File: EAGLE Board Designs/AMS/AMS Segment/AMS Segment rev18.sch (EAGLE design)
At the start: 161 parts, among them J1 CONNECTOR-2_MICROFIT_SMD_RIGH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, J10 CONNECTOR-2_MICROFIT_SMD_RIGH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, J100 CONNECTOR-1_5222_, J101 CONNECTOR-1_5222_, J102 CONNECTOR-1_5222_, J103 CONNECTOR-1_5222_, J104 CONNECTOR-1_5222_, J105 CONNECTOR-1_5222_, J106 CONNECTOR-1_5222_, J107 CONNECTOR-1_5222_, J108 CONNECTOR-1_5222_, J109 CONNECTOR-1_5222_, J110 CONNECTOR-1_5222_, J111 CONNECTOR-1_5222_, J112 CONNECTOR-1_5222_, J113 CONNECTOR-1_5222_, J114 CONNECTOR-1_5222_, J115 CONNECTOR-1_5222_, J116 CONNECTOR-1_5222_, J117 CONNECTOR-1_5222_, J118 CONNECTOR-1_5222_, J119 CONNECTOR-1_5222_, J120 CONNECTOR-1_5222_, J121 CONNECTOR-1_5222_, J2 CONNECTOR-2_MICROFIT_SMD_RIGH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, J3 CONNECTOR-2_MICROFIT_SMD_RIGH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, J4 CONNECTOR-2_MICROFIT_SMD_RIGH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, J5 CONNECTOR-2_MICROFIT_SMD_RIGH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, J6 CONNECTOR-2_MICROFIT_SMD_RIGH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, J7 CONNECTOR-2_MICROFIT_SMD_RIGH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, J8 CONNECTOR-2_MICROFIT_SMD_RIGH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, J9 CONNECTOR-2_MICROFIT_SMD_RIGH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, T1 TRANSFORMER_HM2112ZNLT, U1 SHT31-ARP-B, U2 LTC6811-2, U3 LT3990-5, U4 LT3990-5, U5 LTC6811-2, U6 SHT31-ARP-B

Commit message: Prepped rev 18 with updated lib
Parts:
- J100, J101, J102, J103, J104, J105, J106, J107, J108, J109, J110, J111, J112, J113, J114, J115, J116, J117, J118, J119, J120, J121: value CONNECTOR-1_5222_ -> CONNECTOR-1_5222; device HyTechDevices:CONNECTOR-1_5222_ -> HyTechDevices:CONNECTOR-1_5222
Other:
- note removed: "The LT3990-5 implementation precisely follows the LTC6811-2 datasheet recommendation."
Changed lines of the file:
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@@
 <attribute name="REVIEWER_SCHEMATIC" value="Ethan Weinstock"/>
 </part>
-<part name="Q1" library="HyTechDevices" deviceset="TRANSISTOR_P_MOS_?_*" device="SOT23" technology="SI2369DS-T1-GE3"/>
+<part name="Q1" library="HyTechDevices" deviceset="TRANSISTOR_P_MOS_?_*" device="SOT-23" technology="SI2369DS-T1-GE3"/>
 </parts>
 <sheets>
@@
 <part name="F18" library="HyTechDevices" deviceset="FUSE_?_*" device="0885" technology="1" value="FUSE_0885_1"/>
 <part name="F21" library="HyTechDevices" deviceset="FUSE_?_*" device="0885" technology="1" value="FUSE_0885_1"/>
-<part name="J101" library="HyTechDevices" deviceset="CONNECTOR-1_?_*" device="5222"/>
-<part name="J100" library="HyTechDevices" deviceset="CONNECTOR-1_?_*" device="5222"/>
-<part name="J102" library="HyTechDevices" deviceset="CONNECTOR-1_?_*" device="5222"/>
-<part name="J103" library="HyTechDevices" deviceset="CONNECTOR-1_?_*" device="5222"/>
-<part name="J104" library="HyTechDevices" deviceset="CONNECTOR-1_?_*" device="5222"/>
-<part name="J105" library="HyTechDevices" deviceset="CONNECTOR-1_?_*" device="5222"/>
-<part name="J106" library="HyTechDevices" deviceset="CONNECTOR-1_?_*" device="5222"/>
-<part name="J107" library="HyTechDevices" deviceset="CONNECTOR-1_?_*" device="5222"/>
-<part name="J108" library="HyTechDevices" deviceset="CONNECTOR-1_?_*" device="5222"/>
-<part name="J109" library="HyTechDevices" deviceset="CONNECTOR-1_?_*" device="5222"/>
-<part name="J110" library="HyTechDevices" deviceset="CONNECTOR-1_?_*" device="5222"/>
-<part name="J111" library="HyTechDevices" deviceset="CONNECTOR-1_?_*" device="5222"/>
-<part name="J112" library="HyTechDevices" deviceset="CONNECTOR-1_?_*" device="5222"/>
-<part name="J113" library="HyTechDevices" deviceset="CONNECTOR-1_?_*" device="5222"/>
-<part name="J114" library="HyTechDevices" deviceset="CONNECTOR-1_?_*" device="5222"/>
-<part name="J115" library="HyTechDevices" deviceset="CONNECTOR-1_?_*" device="5222"/>
-<part name="J116" library="HyTechDevices" deviceset="CONNECTOR-1_?_*" device="5222"/>
-<part name="J117" library="HyTechDevices" deviceset="CONNECTOR-1_?_*" device="5222"/>
-<part name="J118" library="HyTechDevices" deviceset="CONNECTOR-1_?_*" device="5222"/>
-<part name="J119" library="HyTechDevices" deviceset="CONNECTOR-1_?_*" device="5222"/>
-<part name="J120" library="HyTechDevices" deviceset="CONNECTOR-1_?_*" device="5222"/>
-<part name="J121" library="HyTechDevices" deviceset="CONNECTOR-1_?_*" device="5222"/>
+<part name="J101" library="HyTechDevices" deviceset="CONNECTOR-1_?" device="5222"/>
+<part name="J100" library="HyTechDevices" deviceset="CONNECTOR-1_?" device="5222"/>
+<part name="J102" library="HyTechDevices" deviceset="CONNECTOR-1_?" device="5222"/>
+<part name="J103" library="HyTechDevices" deviceset="CONNECTOR-1_?" device="5222"/>
+<part name="J104" library="HyTechDevices" deviceset="CONNECTOR-1_?" device="5222"/>
+<part name="J105" library="HyTechDevices" deviceset="CONNECTOR-1_?" device="5222"/>
+<part name="J106" library="HyTechDevices" deviceset="CONNECTOR-1_?" device="5222"/>
+<part name="J107" library="HyTechDevices" deviceset="CONNECTOR-1_?" device="5222"/>
+<part name="J108" library="HyTechDevices" deviceset="CONNECTOR-1_?" device="5222"/>
+<part name="J109" library="HyTechDevices" deviceset="CONNECTOR-1_?" device="5222"/>
+<part name="J110" library="HyTechDevices" deviceset="CONNECTOR-1_?" device="5222"/>
+<part name="J111" library="HyTechDevices" deviceset="CONNECTOR-1_?" device="5222"/>
+<part name="J112" library="HyTechDevices" deviceset="CONNECTOR-1_?" device="5222"/>
+<part name="J113" library="HyTechDevices" deviceset="CONNECTOR-1_?" device="5222"/>
+<part name="J114" library="HyTechDevices" deviceset="CONNECTOR-1_?" device="5222"/>
+<part name="J115" library="HyTechDevices" deviceset="CONNECTOR-1_?" device="5222"/>
+<part name="J116" library="HyTechDevices" deviceset="CONNECTOR-1_?" device="5222"/>
+<part name="J117" library="HyTechDevices" deviceset="CONNECTOR-1_?" device="5222"/>
+<part name="J118" library="HyTechDevices" deviceset="CONNECTOR-1_?" device="5222"/>
+<part name="J119" library="HyTechDevices" deviceset="CONNECTOR-1_?" device="5222"/>
+<part name="J120" library="HyTechDevices" deviceset="CONNECTOR-1_?" device="5222"/>
+<part name="J121" library="HyTechDevices" deviceset="CONNECTOR-1_?" device="5222"/>
 <part name="F20" library="HyTechDevices" deviceset="FUSE_?_*" device="0885" technology="1" value="FUSE_0885_1"/>
 <part name="F22" library="HyTechDevices" deviceset="FUSE_?_*" device="0885" technology="1" value="FUSE_0885_1"/>
@@
 <attribute name="REVIEWER_SCHEMATIC" value="Ethan Weinstock"/>
 </part>
-<part name="O9" library="HyTechExternal" deviceset="PLUG-2_*" device="" technology="MICROFIT_HORIZONTAL"/>
-<part name="O10" library="HyTechExternal" deviceset="PLUG-2_*" device="" technology="MICROFIT_HORIZONTAL"/>
-<part name="O11" library="HyTechExternal" deviceset="PLUG-2_*" device="" technology="MICROFIT_HORIZONTAL"/>
-<part name="O12" library="HyTechExternal" deviceset="PLUG-2_*" device="" technology="MICROFIT_HORIZONTAL"/>
-<part name="O13" library="HyTechExternal" deviceset="PLUG-2_*" device="" technology="MICROFIT_HORIZONTAL"/>
-<part name="O14" library="HyTechExternal" deviceset="PLUG-2_*" device="" technology="MICROFIT_HORIZONTAL"/>
-<part name="O15" library="HyTechExternal" deviceset="PLUG-2_*" device="" technology="MICROFIT_HORIZONTAL"/>
-<part name="O16" library="HyTechExternal" deviceset="PLUG-2_*" device="" technology="MICROFIT_HORIZONTAL"/>
+<part name="O9" library="HyTechExternal" deviceset="RECEPTACLE-2_*" device="" technology="MICROFIT"/>
+<part name="O10" library="HyTechExternal" deviceset="RECEPTACLE-2_*" device="" technology="MICROFIT"/>
+<part name="O11" library="HyTechExternal" deviceset="RECEPTACLE-2_*" device="" technology="MICROFIT"/>
+<part name="O12" library="HyTechExternal" deviceset="RECEPTACLE-2_*" device="" technology="MICROFIT"/>
+<part name="O13" library="HyTechExternal" deviceset="RECEPTACLE-2_*" device="" technology="MICROFIT"/>
+<part name="O14" library="HyTechExternal" deviceset="RECEPTACLE-2_*" device="" technology="MICROFIT"/>
+<part name="O15" library="HyTechExternal" deviceset="RECEPTACLE-2_*" device="" technology="MICROFIT"/>
+<part name="O16" library="HyTechExternal" deviceset="RECEPTACLE-2_*" device="" technology="MICROFIT"/>
 <part name="O17" library="HyTechExternal" deviceset="CRIMP_*" device="" technology="MICROFIT_20-24"/>
 <part name="O18" library="HyTechExternal" deviceset="CRIMP_*" device="" technology="MICROFIT_20-24"/>
@@
 <part name="O23" library="HyTechExternal" deviceset="CRIMP_*" device="" technology="MICROFIT_20-24"/>
 <part name="O24" library="HyTechExternal" deviceset="CRIMP_*" device="" technology="MICROFIT_20-24"/>
-<part name="O1" library="HyTechExternal" deviceset="THERMISTOR" device=""/>
-<part name="O2" library="HyTechExternal" deviceset="THERMISTOR" device=""/>
-<part name="O3" library="HyTechExternal" deviceset="THERMISTOR" device=""/>
-<part name="O4" library="HyTechExternal" deviceset="THERMISTOR" device=""/>
-<part name="O5" library="HyTechExternal" deviceset="THERMISTOR" device=""/>
-<part name="O6" library="HyTechExternal" deviceset="THERMISTOR" device=""/>
-<part name="O7" library="HyTechExternal" deviceset="THERMISTOR" device=""/>
-<part name="O8" library="HyTechExternal" deviceset="THERMISTOR" device=""/>
+<part name="O1" library="HyTechExternal" deviceset="THERMISTOR_*" device="" technology="NTC_LUG"/>
+<part name="O2" library="HyTechExternal" deviceset="THERMISTOR_*" device="" technology="NTC_LUG"/>
+<part name="O3" library="HyTechExternal" deviceset="THERMISTOR_*" device="" technology="NTC_LUG"/>
+<part name="O4" library="HyTechExternal" deviceset="THERMISTOR_*" device="" technology="NTC_LUG"/>
+<part name="O5" library="HyTechExternal" deviceset="THERMISTOR_*" device="" technology="NTC_LUG"/>
+<part name="O6" library="HyTechExternal" deviceset="THERMISTOR_*" device="" technology="NTC_LUG"/>
+<part name="O7" library="HyTechExternal" deviceset="THERMISTOR_*" device="" technology="NTC_LUG"/>
+<part name="O8" library="HyTechExternal" deviceset="THERMISTOR_*" device="" technology="NTC_LUG"/>
 <part name="O25" library="HyTechExternal" deviceset="CRIMP_*" device="" technology="MICROFIT_20-24"/>
 <part name="O26" library="HyTechExternal" deviceset="CRIMP_*" device="" technology="MICROFIT_20-24"/>
@@
 <part name="P94" library="HyTechSupplies" deviceset="V-L" device=""/>
 <part name="P95" library="HyTechSupplies" deviceset="VREGL" device=""/>
-<part name="O33" library="HyTechExternal" deviceset="PLUG-2_*" device="" technology="MICROFIT_HORIZONTAL"/>
-<part name="O34" library="HyTechExternal" deviceset="PLUG-2_*" device="" technology="MICROFIT_HORIZONTAL"/>
+<part name="O33" library="HyTechExternal" deviceset="RECEPTACLE-2_*" device="" technology="MICROFIT"/>
+<part name="O34" library="HyTechExternal" deviceset="RECEPTACLE-2_*" device="" technology="MICROFIT"/>
 <part name="O35" library="HyTechExternal" deviceset="CRIMP_*" device="" technology="MICROFIT_20-24"/>
 <part name="O36" library="HyTechExternal" deviceset="CRIMP_*" device="" technology="MICROFIT_20-24"/>
@@
 <text x="182.88" y="175.26" size="1.27" layer="97">The 100Ω resistor, 10pF capcitor filter is selected
 per the datasheet to maximize GPIO analog accuracy.</text>
-<text x="172.72" y="71.12" size="1.27" layer="97">The LT3990-5 implementation
-precisely follows the LTC6811-2
-datasheet recommendation.</text>
 </plain>
 <moduleinsts>

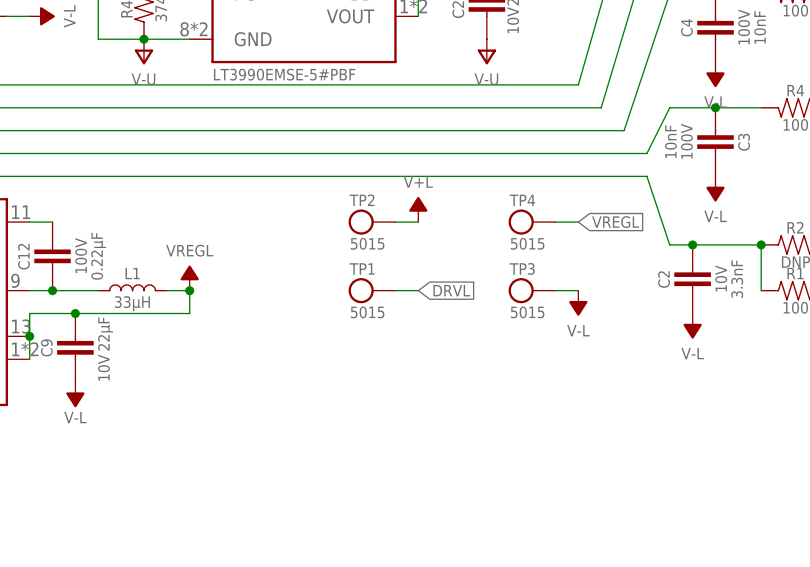
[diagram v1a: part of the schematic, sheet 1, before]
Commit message: Updated testpoints
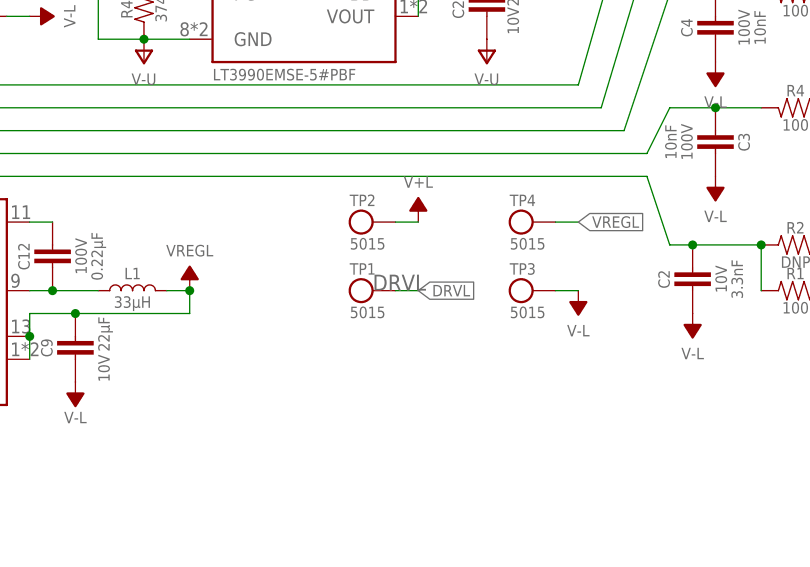
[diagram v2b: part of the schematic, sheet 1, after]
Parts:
- TP1: SIGNAL (none) -> DRVL
- TP10: SIGNAL (none) -> V+U
- TP2: SIGNAL (none) -> V+L
- TP3: SIGNAL (none) -> V-L
- TP4: SIGNAL (none) -> VREGL
- TP5: SIGNAL (none) -> IM
- TP6: SIGNAL (none) -> IP
- TP7: SIGNAL (none) -> V-U
- TP8: SIGNAL (none) -> VREGU
- TP9: SIGNAL (none) -> DRVU
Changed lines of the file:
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@@
 <part name="P66" library="HyTechSupplies" deviceset="VREGU" device=""/>
 <part name="F12" library="HyTechDevices" deviceset="FUSE_?_*" device="0885" technology="1" value="FUSE_0885_1"/>
-<part name="TP9" library="HyTechDevices" deviceset="TEST_POINT" device=""/>
-<part name="TP8" library="HyTechDevices" deviceset="TEST_POINT" device=""/>
-<part name="TP1" library="HyTechDevices" deviceset="TEST_POINT" device=""/>
-<part name="TP4" library="HyTechDevices" deviceset="TEST_POINT" device=""/>
-<part name="TP2" library="HyTechDevices" deviceset="TEST_POINT" device=""/>
-<part name="TP3" library="HyTechDevices" deviceset="TEST_POINT" device=""/>
-<part name="TP10" library="HyTechDevices" deviceset="TEST_POINT" device=""/>
+<part name="TP9" library="HyTechDevices" deviceset="TEST_POINT" device="">
+<attribute name="SIGNAL" value="DRVU"/>
+</part>
+<part name="TP8" library="HyTechDevices" deviceset="TEST_POINT" device="">
+<attribute name="SIGNAL" value="VREGU"/>
+</part>
+<part name="TP1" library="HyTechDevices" deviceset="TEST_POINT" device="">
+<attribute name="SIGNAL" value="DRVL"/>
+</part>
+<part name="TP4" library="HyTechDevices" deviceset="TEST_POINT" device="">
+<attribute name="SIGNAL" value="VREGL"/>
+</part>
+<part name="TP2" library="HyTechDevices" deviceset="TEST_POINT" device="">
+<attribute name="SIGNAL" value="V+L"/>
+</part>
+<part name="TP3" library="HyTechDevices" deviceset="TEST_POINT" device="">
+<attribute name="SIGNAL" value="V-L"/>
+</part>
+<part name="TP10" library="HyTechDevices" deviceset="TEST_POINT" device="">
+<attribute name="SIGNAL" value="V+U"/>
+</part>
 <part name="P27" library="HyTechSupplies" deviceset="V+U" device=""/>
 <part name="P51" library="HyTechSupplies" deviceset="V+L" device=""/>
 <part name="P75" library="HyTechSupplies" deviceset="V-L" device=""/>
-<part name="TP7" library="HyTechDevices" deviceset="TEST_POINT" device=""/>
-<part name="TP6" library="HyTechDevices" deviceset="TEST_POINT" device=""/>
-<part name="TP5" library="HyTechDevices" deviceset="TEST_POINT" device=""/>
+<part name="TP7" library="HyTechDevices" deviceset="TEST_POINT" device="">
+<attribute name="SIGNAL" value="V-U"/>
+</part>
+<part name="TP6" library="HyTechDevices" deviceset="TEST_POINT" device="">
+<attribute name="SIGNAL" value="IP"/>
+</part>
+<part name="TP5" library="HyTechDevices" deviceset="TEST_POINT" device="">
+<attribute name="SIGNAL" value="IM"/>
+</part>
 <part name="P76" library="HyTechSupplies" deviceset="V-U" device=""/>
 <part name="P40" library="HyTechSupplies" deviceset="V-U" device=""/>
@@
 <attribute name="NAME" x="106.68" y="169.418" size="1.27" layer="95"/>
 <attribute name="MPN" x="106.68" y="165.862" size="1.27" layer="95" align="top-left"/>
+<attribute name="SIGNAL" x="109.22" y="167.64" size="1.778" layer="96" display="off"/>
 </instance>
 <instance part="TP8" gate="G$1" x="124.46" y="175.26" smashed="yes">
 <attribute name="NAME" x="121.92" y="177.038" size="1.27" layer="95"/>
 <attribute name="MPN" x="121.92" y="173.482" size="1.27" layer="95" align="top-left"/>
+<attribute name="SIGNAL" x="124.46" y="175.26" size="1.778" layer="96" display="off"/>
 </instance>
 <instance part="TP1" gate="G$1" x="200.66" y="66.04" smashed="yes">
 <attribute name="NAME" x="198.12" y="67.818" size="1.27" layer="95"/>
 <attribute name="MPN" x="198.12" y="64.262" size="1.27" layer="95" align="top-left"/>
+<attribute name="SIGNAL" x="200.66" y="66.04" size="1.778" layer="96"/>
 </instance>
 <instance part="TP4" gate="G$1" x="218.44" y="73.66" smashed="yes">
 <attribute name="NAME" x="215.9" y="75.438" size="1.27" layer="95"/>
 <attribute name="MPN" x="215.9" y="71.882" size="1.27" layer="95" align="top-left"/>
+<attribute name="SIGNAL" x="218.44" y="73.66" size="1.778" layer="96" display="off"/>
 </instance>
 <instance part="TP2" gate="G$1" x="200.66" y="73.66" smashed="yes">
 <attribute name="NAME" x="198.12" y="75.438" size="1.27" layer="95"/>
 <attribute name="MPN" x="198.12" y="71.882" size="1.27" layer="95" align="top-left"/>
+<attribute name="SIGNAL" x="200.66" y="73.66" size="1.778" layer="96" display="off"/>
 </instance>
 <instance part="TP3" gate="G$1" x="218.44" y="66.04" smashed="yes">
 <attribute name="NAME" x="215.9" y="67.818" size="1.27" layer="95"/>
 <attribute name="MPN" x="215.9" y="64.262" size="1.27" layer="95" align="top-left"/>
+<attribute name="SIGNAL" x="218.44" y="66.04" size="1.778" layer="96" display="off"/>
 </instance>
 <instance part="TP10" gate="G$1" x="109.22" y="175.26" smashed="yes">
 <attribute name="NAME" x="106.68" y="177.038" size="1.27" layer="95"/>
 <attribute name="MPN" x="106.68" y="173.482" size="1.27" layer="95" align="top-left"/>
+<attribute name="SIGNAL" x="109.22" y="175.26" size="1.778" layer="96" display="off"/>
 </instance>
 <instance part="P27" gate="G$1" x="114.3" y="177.8" smashed="yes">
@@
 <attribute name="NAME" x="121.92" y="169.418" size="1.27" layer="95"/>
 <attribute name="MPN" x="121.92" y="165.862" size="1.27" layer="95" align="top-left"/>
+<attribute name="SIGNAL" x="124.46" y="167.64" size="1.778" layer="96" display="off"/>
 </instance>
 <instance part="TP6" gate="G$1" x="213.36" y="167.64" smashed="yes">
 <attribute name="NAME" x="210.82" y="169.418" size="1.27" layer="95"/>
 <attribute name="MPN" x="210.82" y="165.862" size="1.27" layer="95" align="top-left"/>
+<attribute name="SIGNAL" x="213.36" y="167.64" size="1.778" layer="96" display="off"/>
 </instance>
 <instance part="TP5" gate="G$1" x="213.36" y="121.92" smashed="yes">
 <attribute name="NAME" x="210.82" y="123.698" size="1.27" layer="95"/>
 <attribute name="MPN" x="210.82" y="120.142" size="1.27" layer="95" align="top-left"/>
+<attribute name="SIGNAL" x="213.36" y="121.92" size="1.778" layer="96" display="off"/>
 </instance>
 <instance part="P76" gate="G$1" x="134.62" y="165.1" smashed="yes">
